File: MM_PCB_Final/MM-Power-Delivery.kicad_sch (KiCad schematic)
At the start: 6 parts, among them J7 JST Connector, J8 JST Connector, U8 Voltage Regulator

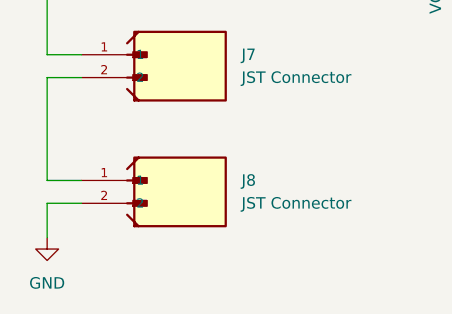
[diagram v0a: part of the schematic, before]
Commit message: fix mgnd and gnd short
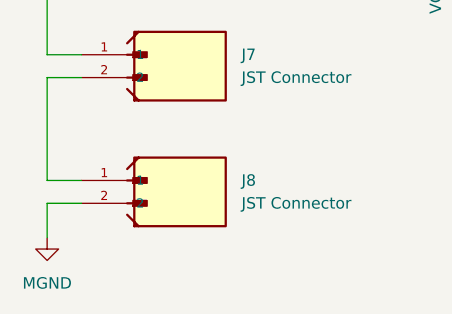
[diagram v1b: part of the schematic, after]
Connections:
- net GND: no longer J8.2
- new net MGND: J8.2
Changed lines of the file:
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@@
 			)
 		)
-		(property "Value" "GND"
+		(property "Value" "MGND"
 			(at 74.93 123.19 0)
 			(effects
